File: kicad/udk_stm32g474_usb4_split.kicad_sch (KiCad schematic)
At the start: 146 parts, among them J1 USB_A, J10 QWIIC, J11 ARGB, J12 5V, J13 USB_C_Receptacle, J14 Conn_01x08_Pin, J15 Conn_01x08_Pin, J16 TC2030-SWD, J17 Conn_01x02_Socket, J18 Conn_01x02_Socket, J2 USB_A, J5 USB_A, J8 SPI, J9 CONN, Q1 AO3401A, SW1 BOOT, SW2 RESET, U1 TS3USB30ERSWR, U10 REF3033E, U11 CH217K, U12 M25C-MEM-SPI, U13 TS3USB30ERSWR, U14 TS3USB30ERSWR, U15 TS3USB30ERSWR, U16 TS3USB30ERSWR, U17 LM66100DCK, U18 LM66100DCK, U19 LM66100DCK, U2 MCP23008-xML, U20 LP5907MFX-3.3, U21 NC7SZ125M5X, U22 LM66100DCK, U23 24AA02E48-OT, U3 CH334F, U4 LM66100DCK, U5 LM66100DCK, U6 STM32G474CBTx, U7 TS3USB30ERSWR, U8 LM66100DCK, U9 LM66100DCK, X1 Qwicc Logo, X2 Tecsmith Logo, X3 UDK Logo, X4 OSHW Logo, Y1 12MHz SMD3225-4P, Y2 8MHz SMD3225-4P

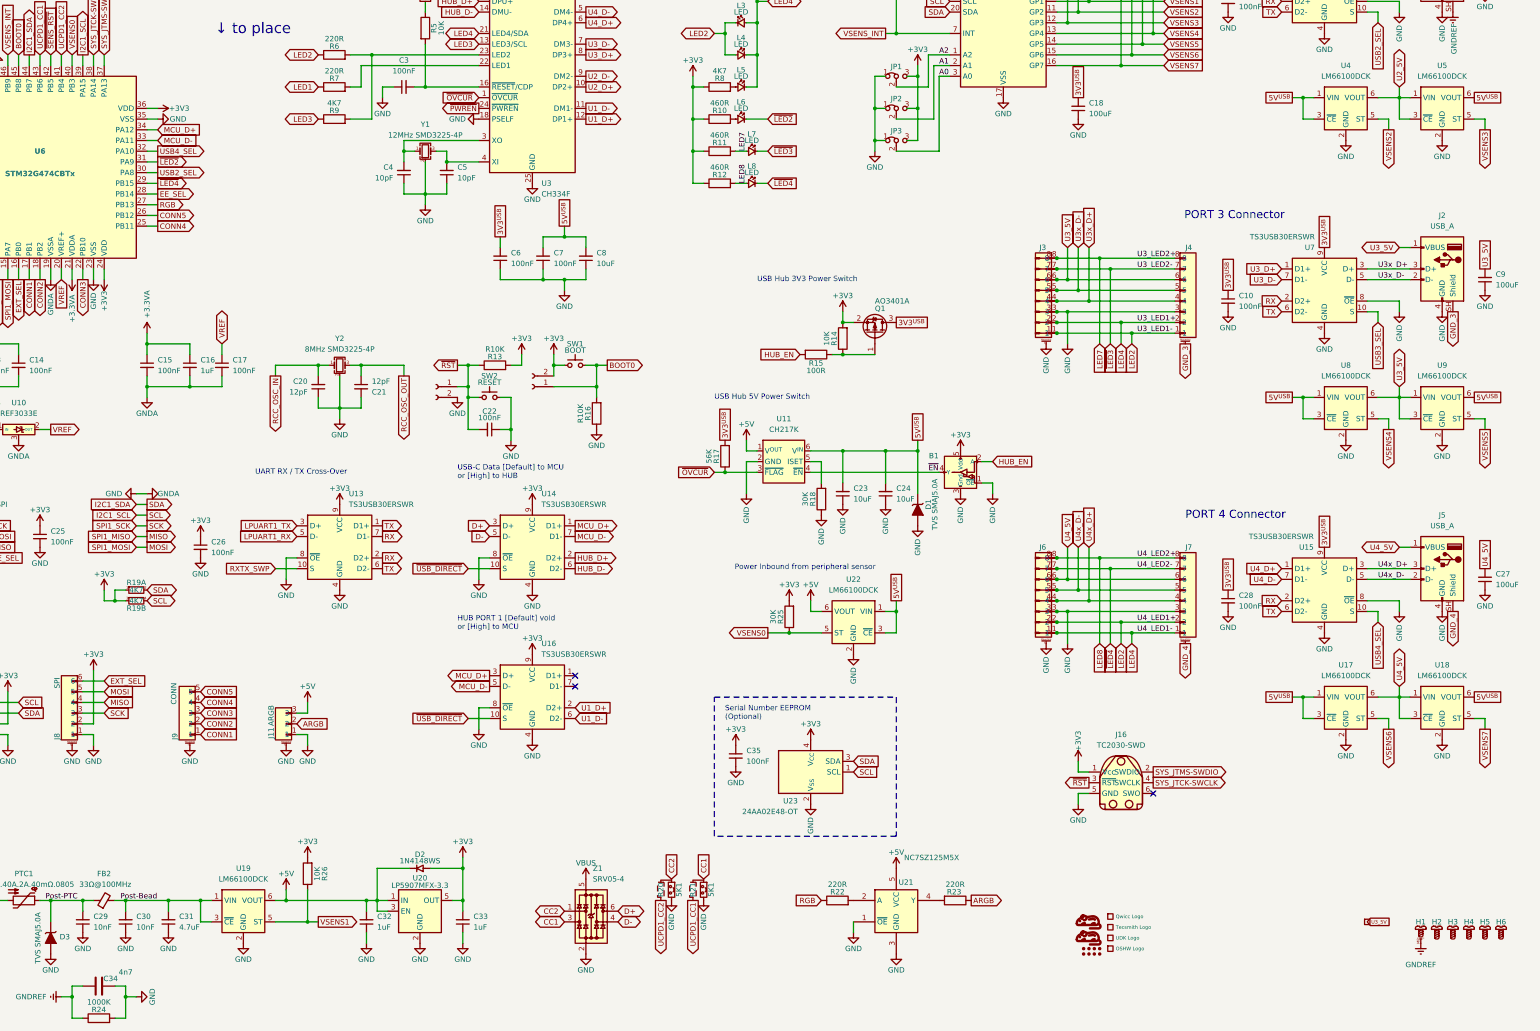
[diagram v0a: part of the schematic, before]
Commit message: added port esd
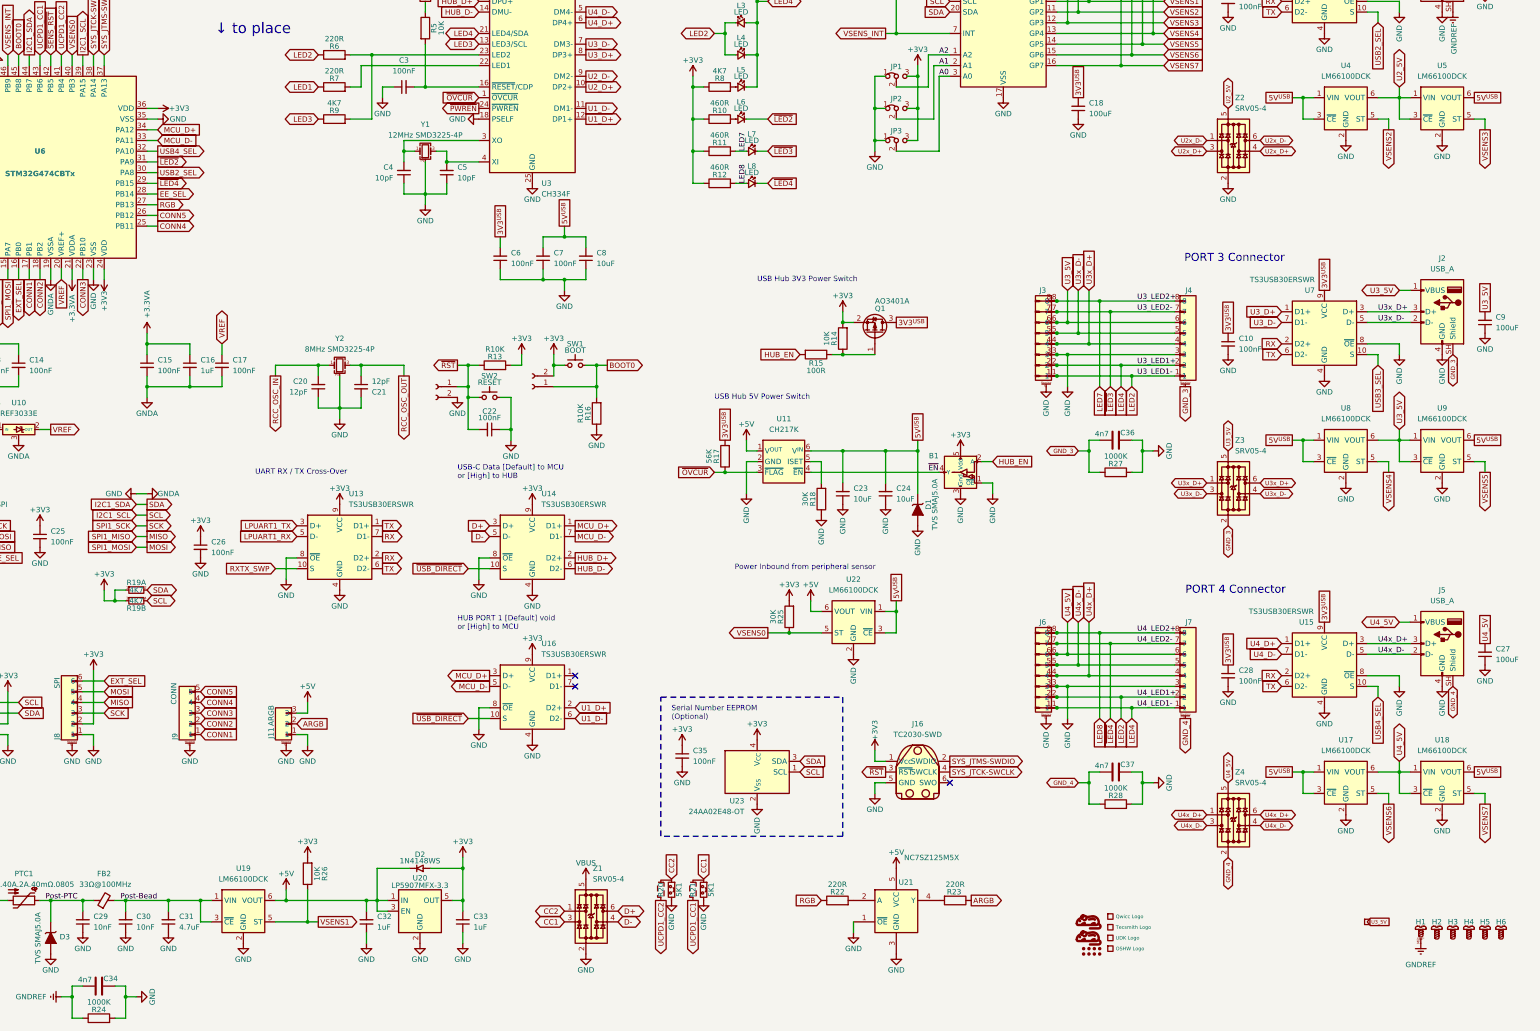
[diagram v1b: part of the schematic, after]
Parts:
- added C36, C37: 4n7, Capacitor_SMD:C_0805_2012Metric_Pad1.18x1.45mm_HandSolder, symbol Device:C
- added R27, R28: 1000K, Resistor_SMD:R_0805_2012Metric, symbol Device:R
- added Z2, Z3, Z4: SRV05-4, Package_SO:TSOP-6_1.65x3.05mm_P0.95mm, symbol ts-kicad-lib:SRV05-4
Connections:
- net GND: now also C36.2, C37.2, R27.2, R28.2, Z2.2
- net GND_3: now also C36.1, R27.1, Z3.2
- net GND_4: now also C37.1, R28.1, Z4.2
- net U2_5V: now also Z2.5
- net U2x_D+: now also Z2.3, Z2.4
- net U2x_D-: now also Z2.1, Z2.6
- net U3_5V: now also Z3.5
- net U3x_D+: now also Z3.1, Z3.6
- net U3x_D-: now also Z3.3, Z3.4
- net U4_5V: now also Z4.5
- net U4x_D+: now also Z4.1, Z4.6
- net U4x_D-: now also Z4.3, Z4.4
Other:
- moved on the sheet: C10, C27, C28, C35, C9, J16, J2, J3, J4, J5, J6, J7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
